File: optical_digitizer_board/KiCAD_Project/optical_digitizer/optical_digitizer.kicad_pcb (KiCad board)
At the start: 4 copper layers, 114.3 x 33 mm, 40 parts, among them J1 Female Input Connector, J2 Male Output Connector, U1 LM358AP, U2 LM358AP, U3 MCP3202

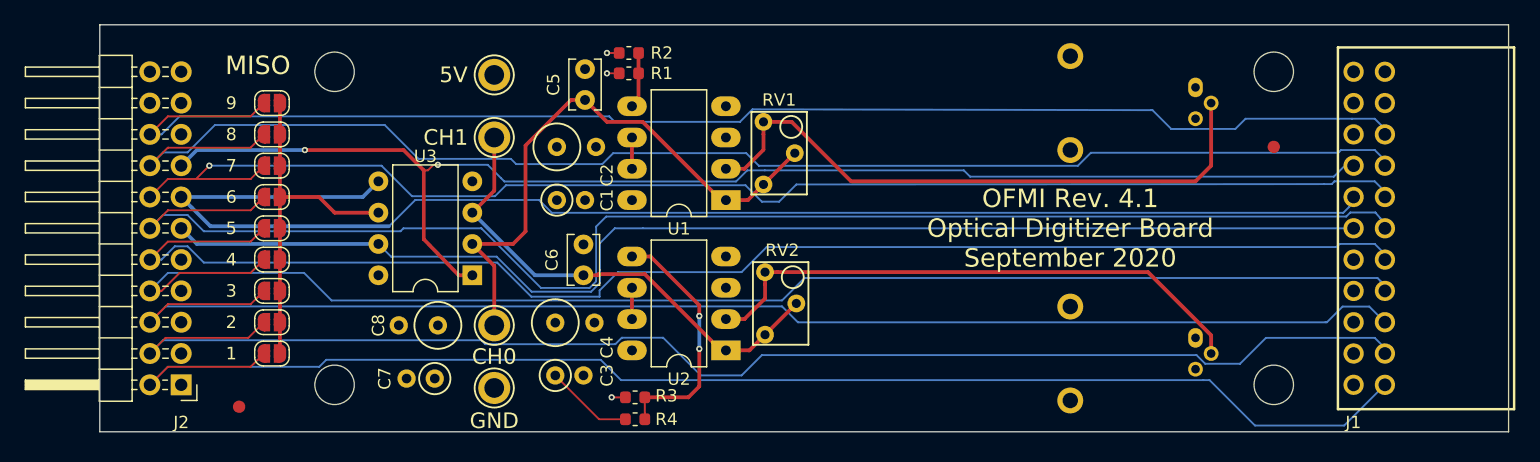
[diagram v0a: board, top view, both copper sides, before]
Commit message: Revise optical digitizer to Rev 4.2
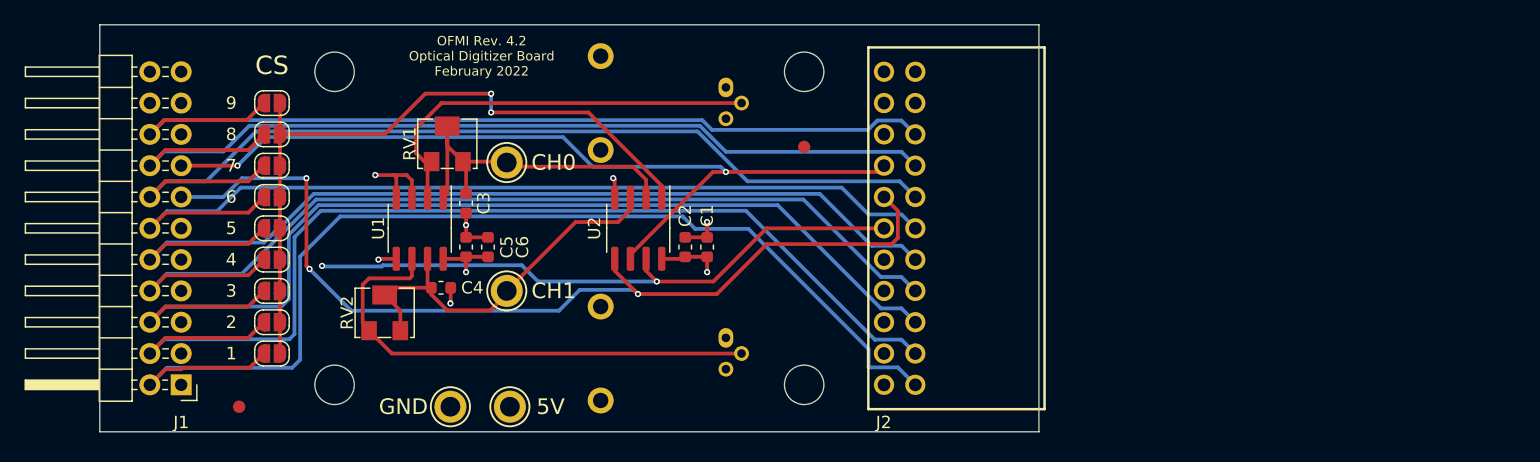
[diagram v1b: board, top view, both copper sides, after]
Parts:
- removed C7: 0.1uF, lib_fp:2.54x4.32CAP
- removed C8: 1uF, lib_fp:3.81x10.16CAP
- removed R1, R2, R3, R4: 10k, Resistor_SMD:R_0603_1608Metric
- removed U3: MCP3202, Housings_DIP:DIP-8_W7.62mm
- added PCB1: barepcb, misc:barepcb, F.Cu at (148.8, 154.7)
- C1: value 0.1uF -> 1-0000007; footprint lib_fp:2.54x4.32CAP -> capacitors_0603:1-0000007
- C2: value 1uF -> 1-0000018; footprint lib_fp:3.81x10.16CAP -> capacitors_0603:1-0000018
- C3: value 0.1uF -> 1-0001030; footprint lib_fp:2.54x4.32CAP -> capacitors_0603:1-0001030
- C4: value 1uF -> 1-0001030; footprint lib_fp:3.81x10.16CAP -> capacitors_0603:1-0001030
- C5: value 1pF -> 1-0000007; footprint Capacitors_THT:C_Rect_L4.0mm_W2.5mm_P2.50mm -> capacitors_0603:1-0000007
- C6: value 1pF -> 1-0000018; footprint Capacitors_THT:C_Rect_L4.0mm_W2.5mm_P2.50mm -> capacitors_0603:1-0000018
- RV1, RV2: value 100k -> 1-0001029; footprint lib_fp:3266W -> resistors_variable:1-0001029
- U1: value LM358AP -> 1-0001027; footprint Package_DIP:DIP-8_W7.62mm_LongPads -> amplifiers:1-0001027
- U2: value LM358AP -> 1-0001028; footprint Package_DIP:DIP-8_W7.62mm_LongPads -> adcs:1-0001028
- moved D1 38.1 mm to (127.0, 124.5)
- moved D2 38.1 mm to (127.0, 144.8)
- moved FID2 38.1 mm to (133.3, 129.3)
- moved H2 38.1 mm to (133.3, 123.2)
- moved H3 38.1 mm to (133.3, 148.6)
- moved J2 38.1 mm to (148.1, 135.9)
- moved RV2 32.1 mm to (99.3, 142.7)
- moved TP3 27.0 mm to (109.5, 150.4)
- moved RV1 26.9 mm to (104.4, 129.0)
- moved U1 24.9 mm to (102.2, 135.9), turned to 270 degrees
- moved C3 15.7 mm to (105.9, 133.9)
- moved C5 15.4 mm to (105.9, 137.4), turned to 270 degrees
- moved TP1 13.2 mm to (109.2, 130.6)
- moved C2 13.2 mm to (123.7, 137.4)
- moved C1 12.8 mm to (125.5, 137.4)
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- renumbered J2 to J1, J1 to J2, TP3 to TP1, TP4 to TP2, TP1 to TP3, TP2 to TP4
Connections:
- net /MISO1 renamed /CS1
- net /MISO2 renamed /CS2
- net /MISO3 renamed /CS3
- net /MISO4 renamed /CS4
- net /MISO5 renamed /CS5
- net /MISO6 renamed /CS6
- net /MISO7 renamed /CS7
- net /MISO8 renamed /CS8
- net /MISO9 renamed /CS9
- C3 pad 1: GND -> Net-(C3-Pad1)
- C3 pad 2: +5V -> GND
- C4 pad 1: GND -> Net-(C4-Pad1)
- C4 pad 2: +5V -> GND
- C5 pad 1: Net-(C5-Pad1) -> GND
- C5 pad 2: GND -> +5V
- C6 pad 1: Net-(C6-Pad1) -> GND
- C6 pad 2: GND -> +5V
- J1 pad 15: /CS -> /MISO
- J2 pad 15: /CS -> /MISO
- JP1 pad 1: /MISO -> /CS
- JP2 pad 1: /MISO -> /CS
- JP3 pad 1: /MISO -> /CS
- JP4 pad 1: /MISO -> /CS
- JP5 pad 1: /MISO -> /CS
- JP6 pad 1: /MISO -> /CS
- JP7 pad 1: /MISO -> /CS
- JP8 pad 1: /MISO -> /CS
- JP9 pad 1: /MISO -> /CS
- RV1 pad 2: Net-(C5-Pad1) -> Net-(C3-Pad1)
- RV1 pad 3: Net-(C5-Pad1) -> Net-(C3-Pad1)
- RV2 pad 2: Net-(C6-Pad1) -> Net-(C4-Pad1)
- RV2 pad 3: Net-(C6-Pad1) -> Net-(C4-Pad1)
- TP1 pad 1: Net-(C5-Pad1) -> Net-(C3-Pad1)
- TP2 pad 1: Net-(C6-Pad1) -> Net-(C4-Pad1)
- U1 pad 1: Net-(C5-Pad1) -> Net-(C3-Pad1)
- U1 pad 5: Net-(R1-Pad2) -> GND
- U1 pad 6: Net-(U1-Pad6) -> Net-(D2-Pad2)
- U1 pad 7: Net-(U1-Pad6) -> Net-(C4-Pad1)
- U2 pad 1: Net-(C6-Pad1) -> /CS
- U2 pad 2: Net-(D2-Pad2) -> Net-(C3-Pad1)
- U2 pad 3: GND -> Net-(C4-Pad1)
- U2 pad 5: Net-(R3-Pad2) -> /MOSI
- U2 pad 6: Net-(U2-Pad6) -> /MISO
- U2 pad 7: Net-(U2-Pad6) -> /SCLK
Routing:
- net /CS: track 109.2 -> 57.6 mm
- net Net-(C5-Pad1): track 47.4 -> 0.00 mm
- net /CS6: track 119.8 -> 75.1 mm
- net /MISO: track 28.8 -> 70.2 mm, vias 0 -> 2
- net /CS9: track 115.4 -> 74.0 mm
- net /CS8: track 115.5 -> 75.1 mm
- net Net-(C6-Pad1): track 39.4 -> 0.00 mm
- net /CS5: track 115.7 -> 76.8 mm
- net /SCLK: track 101.7 -> 62.9 mm, vias 0 -> 2
- net /MOSI: track 114.9 -> 77.5 mm, vias 0 -> 3
- net /CS4: track 113.7 -> 78.6 mm
- net /CS7: track 110.7 -> 76.8 mm, vias 1 -> 0
- net Net-(C4-Pad1): track 0.00 -> 31.8 mm
- net /CS3: track 112.6 -> 83.3 mm
- net Net-(C3-Pad1): track 0.00 -> 29.0 mm
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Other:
- board size 114.3 x 33 mm -> 76.2 x 33 mm
- rule pad_to_mask_clearance: 0.0508 -> 0
- board text added: "3-0000125"
- board text added: "CS1"
- board text added: "CS2"
- board text added: "CS3"
- board text added: "CS4"
- board text added: "CS5"
- board text added: "CS6"
- board text added: "CS7"
- board text added: "CS8"
- board text added: "CS9"
- board text added: "OFMI Rev. 4.2 Optical Digitizer Board February 2022"
- board text removed: "LG 3-0000045"
- board text removed: "MISO1"
- board text removed: "MISO2"
- board text removed: "MISO3"
- board text removed: "MISO4"
- board text removed: "MISO5"
- board text removed: "MISO6"
- board text removed: "MISO7"
- board text removed: "MISO8"
- board text removed: "MISO9"
- board text removed: "OFMI Rev. 4.1 Optical Digitizer Board September 2020"
